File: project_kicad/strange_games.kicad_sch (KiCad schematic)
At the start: 156 parts, among them J1 Display, J2 Conn_02x02, J3 Conn_02x02, M1 Motor_DC, Q1 Q_Photo_NPN, Q2 Q_Photo_NPN, Q3 Si2302A, Q4 Si2302A, SW1 SW_Push, SW10 SW_Push, SW11 SW_Push, SW12 SW_Push, SW2 SW_Push, SW3 SW_Push, SW4 SW_Push, SW5 SW_Push, SW6 SW_Push, SW7 SW_Push, SW8 SW_Push, SW9 SW_Push, U1 STM32F446ZET6, U2 charge controller, U3 boost converter, U4 LDL1117S33R, U5 MQ-135 gas sensor, U6 ESP8266-01, U7 TMP112xxDRL, U8 LSM6DS3

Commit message: replaces stm32 with esp32
remade schematic, replacing stm32 with esp32, starting making pcb. Deleted projects for stm32 and esp8266
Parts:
- removed C10, C11, C12, C13, C14, C15, C16, C18, C19, C20, C42, C45, C6, C68, C7, C8: C_Generic, PCM_Capacitor_SMD_AKL:C_0402_1005Metric, symbol Library:C_Generic
- removed C17, C43, C66, C9: C_Generic, PCM_Capacitor_SMD_AKL:C_0805_2012Metric, symbol Library:C_Generic
- removed FB1: FerriteBead, Inductor_SMD:L_0805_2012Metric, symbol Library:FerriteBead
- removed J2, J3: Conn_02x02, Connector_PinHeader_2.54mm:PinHeader_2x02_P2.54mm_Vertical, symbol Library:Conn_02x03
- removed R1, R15, R19, R2, R22, R23, R24, R4, R5: 10k_0805, PCM_4ms_Resistor:R_0805_2012Metric, symbol Library:1.2k_0603
- removed U1: STM32F446ZET6, Package_QFP:LQFP-144_20x20mm_P0.5mm, symbol Library:STM32F446ZETx
- removed U6: ESP8266-01, SnapEDA Library:XCVR_ESP8266-01_ESP-01, symbol Library:ESP8266-01/ESP-01
- added C70, C71: C_Generic, PCM_Capacitor_SMD_AKL:C_0402_1005Metric, symbol Library:C_Generic
- added C72: C_Generic, PCM_Capacitor_SMD_AKL:C_0805_2012Metric, symbol Library:C_Generic
- added R43, R44, R45, R46, R47: 10k_0805, PCM_4ms_Resistor:R_0805_2012Metric, symbol Library:1.2k_0603
- added U10: vibrating_sensor, symbol Sensor:vibarting_sensor
- added U9: ESP32-DEVKIT-V1, SnapEDA Library:MODULE_ESP32_DEVKIT_V1, symbol ESP32-DEVKIT-V1:ESP32-DEVKIT-V1
- C1: footprint PCM_Capacitor_SMD_AKL:C_0402_1005Metric -> PCM_Capacitor_SMD_AKL:C_0805_2012Metric; Capacity 2.2uF -> 10uF; Display ?F -> (none)
- C3, C4: footprint PCM_Capacitor_SMD_AKL:C_0402_1005Metric -> PCM_Capacitor_SMD_AKL:C_0805_2012Metric; Capacity 0.1uF -> 10uF; Voltage 10V -> 6.3V
- Q1, Q2: value Q_Photo_NPN -> Q_Photo
- U5: footprint Library:MQ-135 gas sensor -> Connector_PinHeader_1.27mm:PinHeader_1x04_P1.27mm_Vertical
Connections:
- net +3.3VA is gone; now on net +3V3: C5.1
- net CS_lsm is gone; now on net +3V3: U8.12 (CS)
- net SCL_lsm is gone; now on net SCL: U8.13 (SCL)
- net SCL_tmp is gone; now on net SCL: U7.1 (SCL)
- net SDA_lsm is gone; now on net SDA: U8.14 (SDA)
- net +3V3: now also C1.2, C2.1, C4.2, U5.1 (VCC), C70.2, C71.1, C72.2, R43.2, R44.2, R45.2, R46.2, R47.2, U10.1 (VCC), U9.1 (3V3), U9.16 (EN); no longer C4.1, J1.3 (P/S), R13.2, U5.2 (VCC)
- net B1: now also U9.22 (D33)
- net B10: now also U9.12 (RX0)
- net B11: now also U9.18 (VN)
- net B12: now also U9.17 (VP)
- net B2: now also U9.21 (D32)
- net B3: now also U9.25 (D27)
- net B4: now also U9.24 (D26)
- net B5: now also U9.23 (D25)
- net B6: now also U9.15 (D23)
- net B7: now also U9.7 (TX2)
- net B8: now also U9.6 (RX2)
- net B9: now also U9.13 (TX0)
- net GND: now also C2.2, C4.1, J1.3 (P/S), R13.1, U5.2 (GND), C70.1, C71.2, C72.1, U10.2 (GND), U9.2 (GND), U9.29 (GND__1); no longer C2.1, C4.2, U5.1 (GND)
- net at D10.4 (DI): now also D9.1 (DO); no longer D7.1 (DO)
- net at D12.1 (DO): now also D9.4 (DI); no longer D7.4 (DI)
- net at D12.4 (DI): now also D7.1 (DO); no longer D9.1 (DO)
- net at D6.1 (DO): now also D7.4 (DI); no longer D9.4 (DI)
- net C15 renamed gas_signal
- net gas_signal: now also U9.26 (D14), U9.8 (D5)
- net C2 renamed open_box
- net open_box: now also U9.19 (D34)
- net D0 renamed A0_display
- net A0_display: now also R45.1, U9.3 (D15)
- net D1 renamed WR_display
- net WR_display: now also R46.1, U9.9 (D18)
- net D10 renamed SDA
- net SDA: now also U7.6 (SDA), R43.1, U9.11 (D21)
- net D2 renamed RD_display
- net RD_display: now also R47.1, U9.10 (D19)
- net D3: no longer names the net of J1.29 (D0)
- net D4: no longer names the net of J1.28 (D1)
- net D5: no longer names the net of J1.27 (D2)
- net D6: no longer names the net of J1.26 (D3)
- net D7: no longer names the net of J1.25 (D4)
- net D8: no longer names the net of J1.24 (D5)
- net D9 renamed SCL
- net SCL: now also R44.1, U9.14 (D22)
- removed net SDA_tmp: R13.1, U7.6 (SDA)
- net С0 renamed luminodiodes
- net luminodiodes: now also U9.4 (D2)
- net С1 renamed vibrating_motor
- net vibrating_motor: now also U9.20 (D35)
- net С3 renamed photo_1
- net photo_1: now also U9.28 (D13)
- net С4 renamed photo_2
- net photo_2: now also U9.27 (D12)
- new net vibrating_signal: R13.2, U10.3 (DO), U9.5 (D4)
- no-connect marks 7 -> 14
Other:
- note added: "ESP32 для управления всем кубиком и связи по wifi"
- note added: "датчики цифровые должны быть близко к ESP32 датчики света отдельно"
- note removed: "VBAT"
- note removed: "VDD"
- note removed: "VDDA"
- note removed: "esp8266 для бутлодера и общения по wi-fi"
- note removed: "stm32 для управления всей игрой"
- note removed: "датчики цифровые должны быть близко к stm32 датчики света отдельно"
- moved on the sheet: BT1, C21, C22, C23, C24, C25, C26, C27, C28, C29, C30, C31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

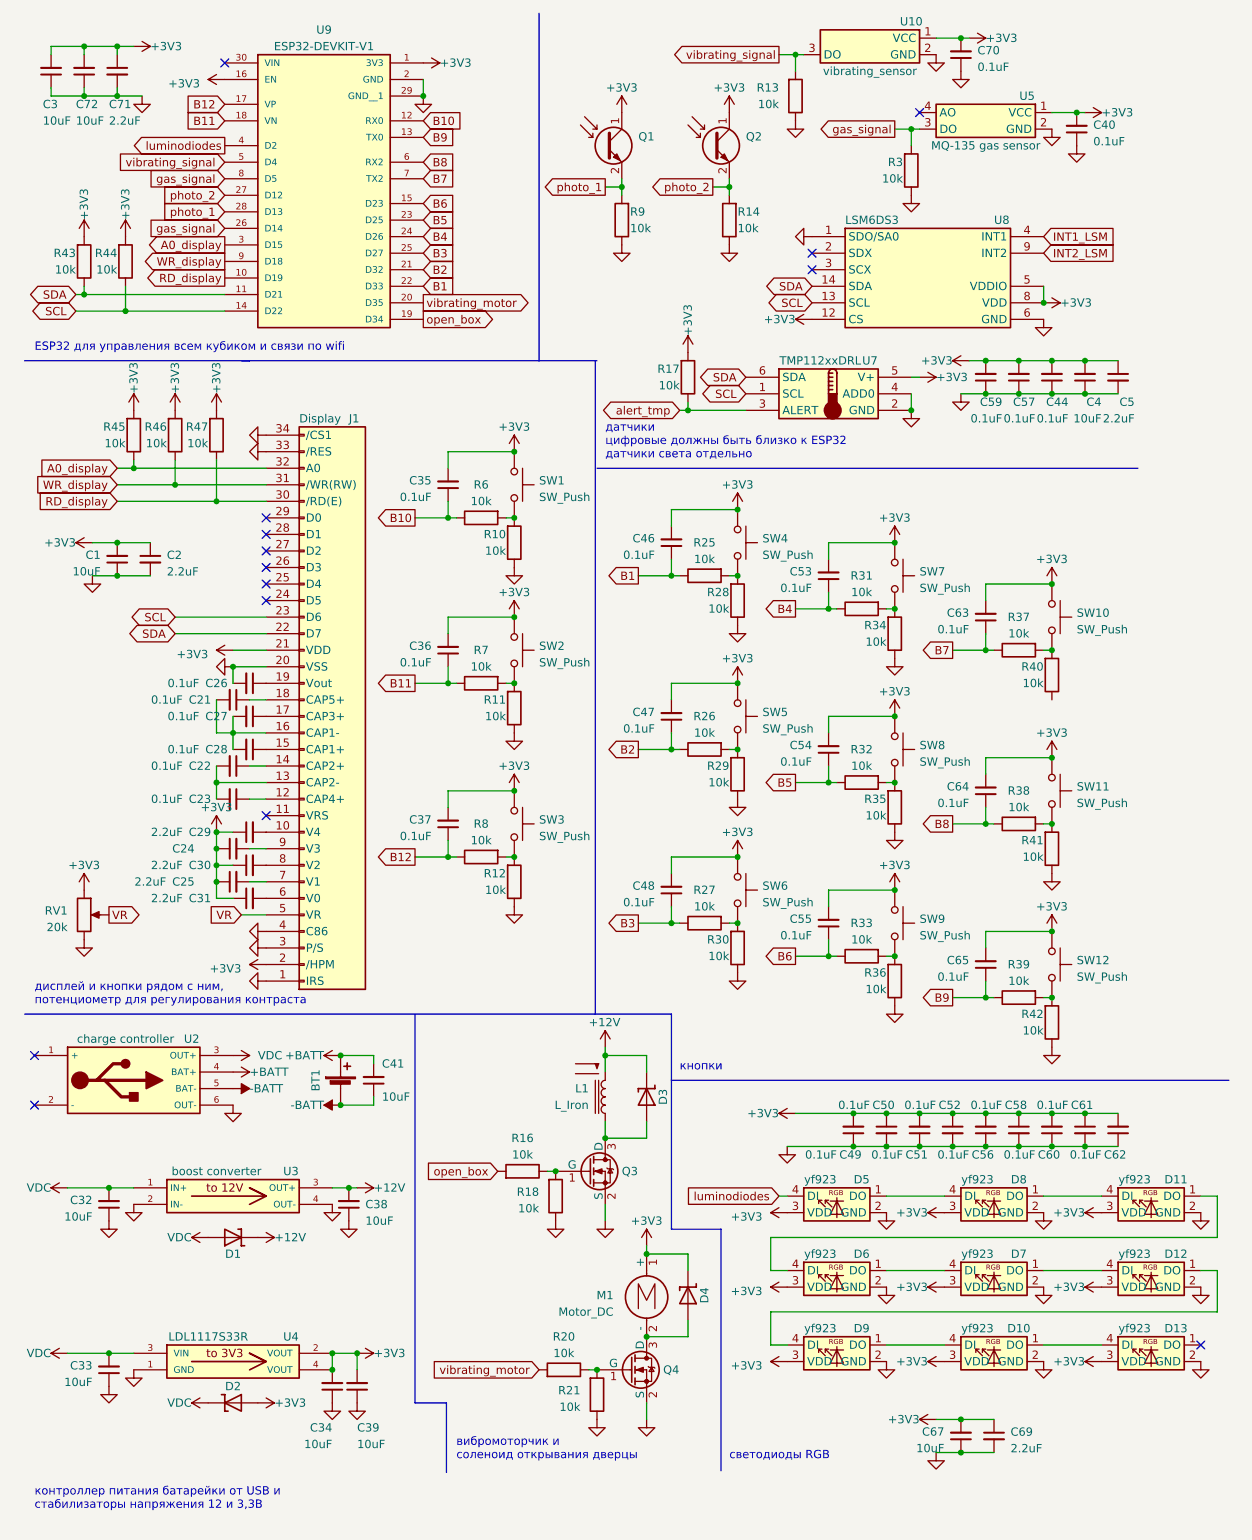
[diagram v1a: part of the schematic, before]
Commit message: updated components numbers
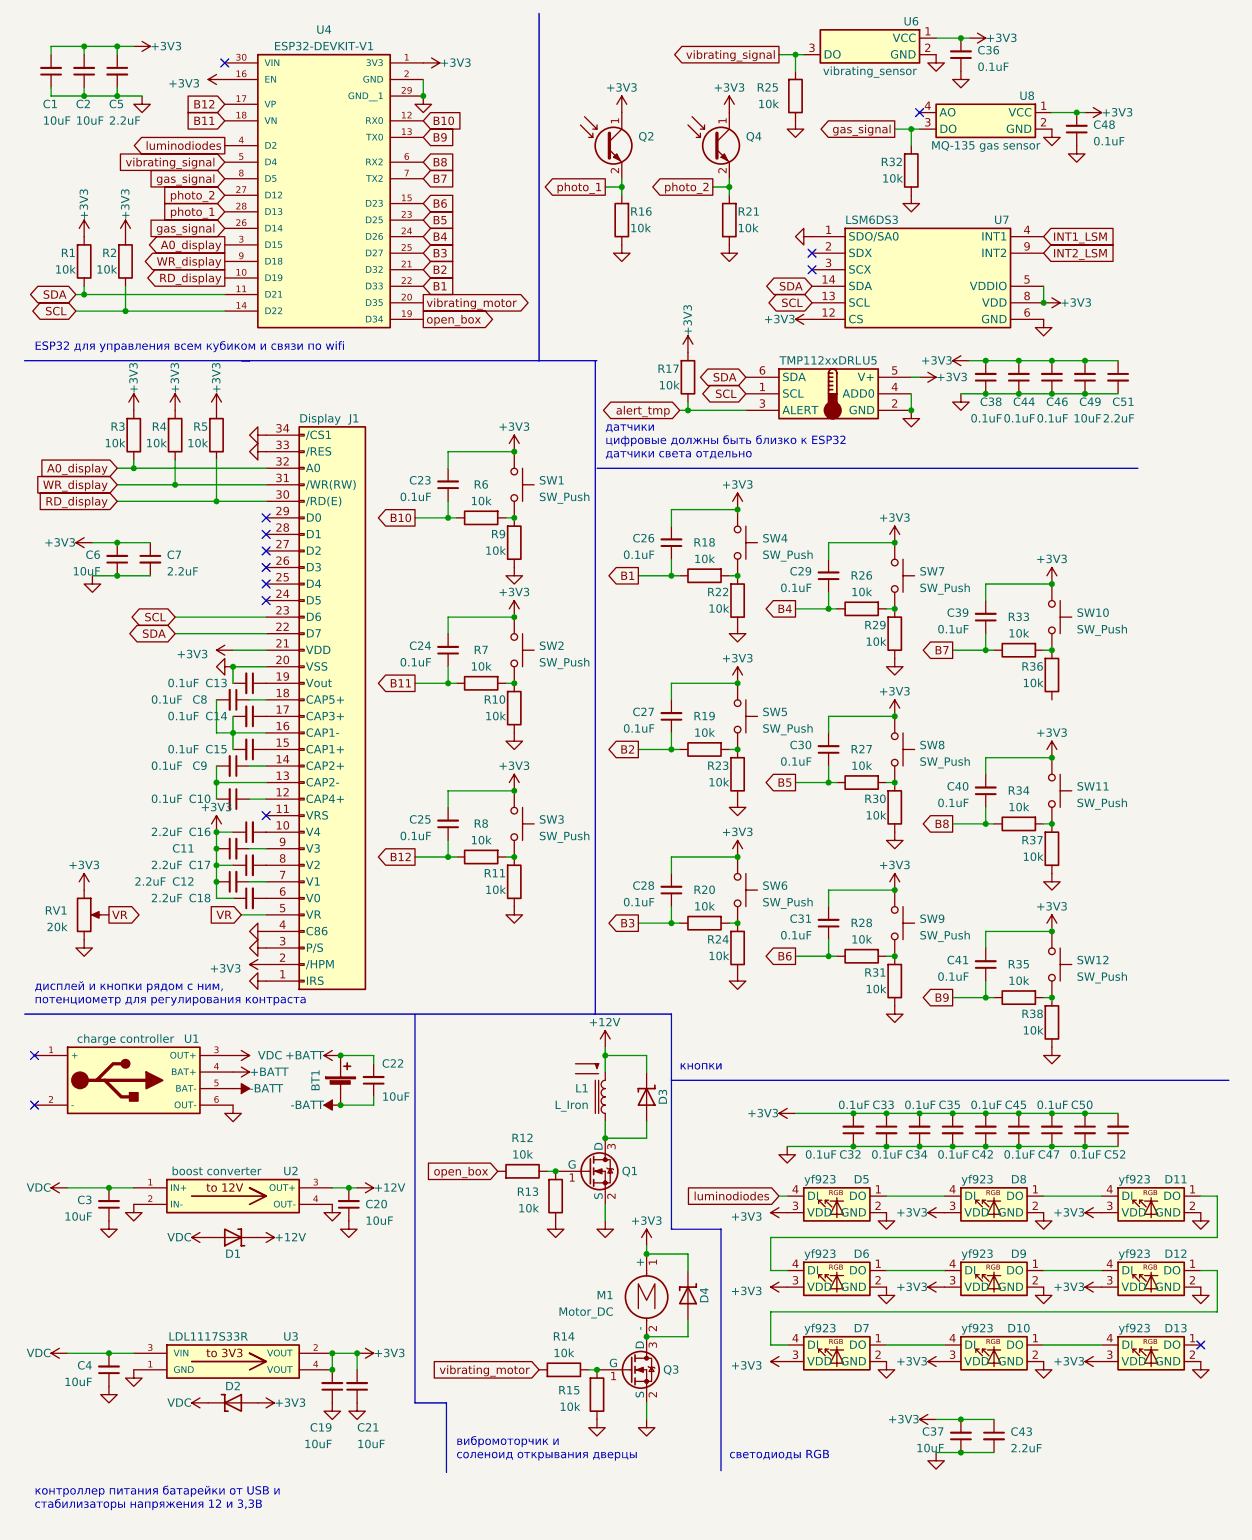
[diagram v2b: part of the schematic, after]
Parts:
- renumbered C3 to C1, C23 to C10, C24 to C11, C25 to C12, C26 to C13, C27 to C14, C28 to C15, C29 to C16, C30 to C17, C31 to C18, C34 to C19, C72 to C2, C38 to C20, C39 to C21, C41 to C22, C35 to C23, C36 to C24, C37 to C25, C46 to C26, C47 to C27, C48 to C28, C53 to C29, C32 to C3, C54 to C30, C55 to C31, C49 to C32, C50 to C33, C51 to C34, C52 to C35, C70 to C36, C67 to C37, C59 to C38, C63 to C39, C33 to C4, C64 to C40, C65 to C41, C56 to C42, C69 to C43, C57 to C44, C58 to C45, C44 to C46, C60 to C47, C40 to C48, C4 to C49, C71 to C5, C61 to C50, C5 to C51, C62 to C52, C1 to C6, C2 to C7, C21 to C8, C22 to C9, D9 to D7, D7 to D9, Q3 to Q1, Q1 to Q2, Q4 to Q3, Q2 to Q4, R43 to R1, R11 to R10, R12 to R11, R16 to R12, R18 to R13, R20 to R14, R21 to R15, R9 to R16, R25 to R18, R26 to R19, R44 to R2, R27 to R20, R14 to R21, R28 to R22, R29 to R23, R30 to R24, R13 to R25, R31 to R26, R32 to R27, R33 to R28, R34 to R29, R45 to R3, R35 to R30, R36 to R31, R3 to R32, R37 to R33, R38 to R34, R39 to R35, R40 to R36, R41 to R37, R42 to R38, R46 to R4, R47 to R5, R10 to R9, U2 to U1, U3 to U2, U4 to U3, U9 to U4, U7 to U5, U10 to U6, U8 to U7, U5 to U8

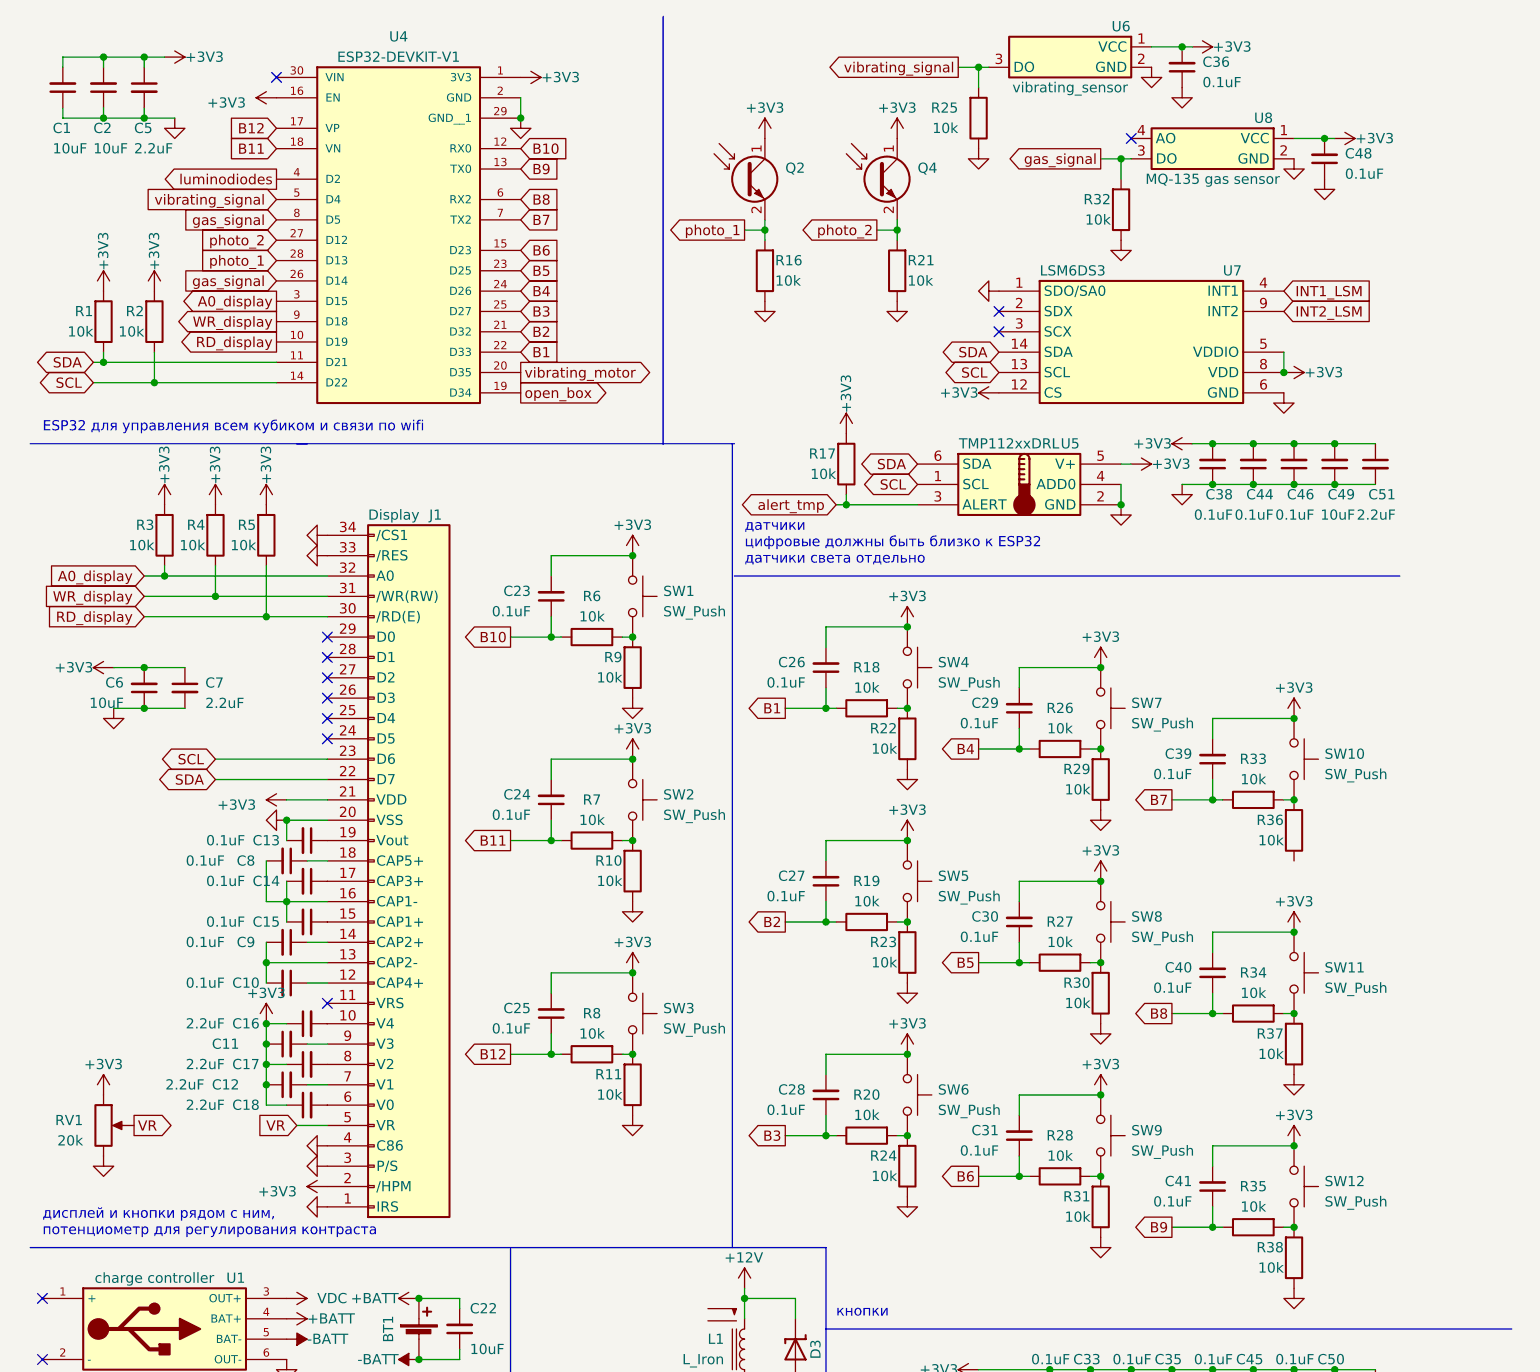
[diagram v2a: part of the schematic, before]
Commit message: deleted pins
deleted temperature alert pin and 2 buttons near the display because there are no enough pins in esp32
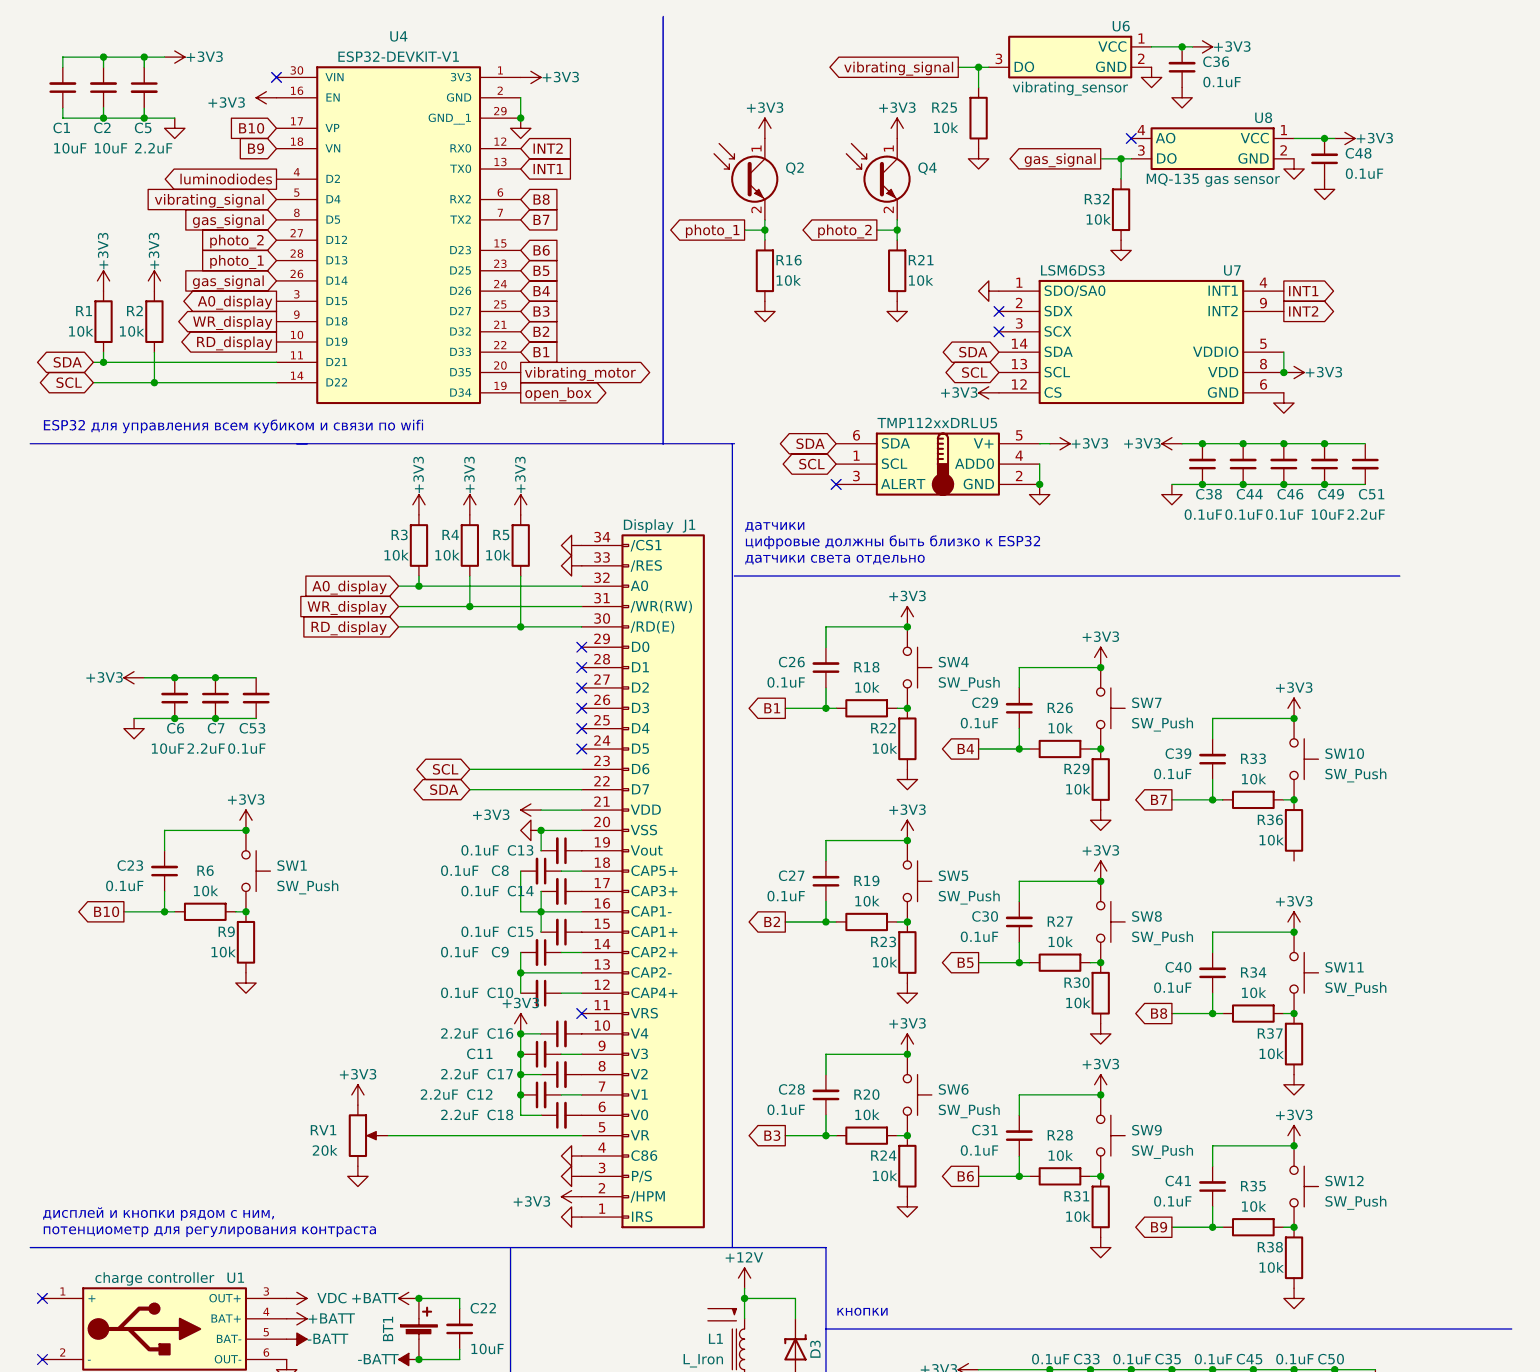
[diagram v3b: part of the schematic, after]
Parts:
- removed C24, C25: C_Generic, PCM_Capacitor_SMD_AKL:C_0402_1005Metric, symbol Library:C_Generic
- removed R10, R11, R17, R7, R8: 10k_0805, PCM_4ms_Resistor:R_0805_2012Metric, symbol Library:1.2k_0603
- removed SW2, SW3: SW_Push, Button_Switch_THT:SW_PUSH-12mm, symbol Switch:SW_Push
- added C53: C_Generic, PCM_Capacitor_SMD_AKL:C_0402_1005Metric, symbol Library:C_Generic
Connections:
- net B11 is gone; now on net B9: U4.18 (VN)
- net B12 is gone; now on net B10: U4.17 (VP)
- net +3V3: now also C53.2
- net B10: no longer U4.12 (RX0)
- net B9: no longer U4.13 (TX0)
- net GND: now also C53.1
- net INT1_LSM renamed INT1
- net INT1: now also U4.13 (TX0)
- net INT2_LSM renamed INT2
- net INT2: now also U4.12 (RX0)
- net VR: no longer names the net of J1.5 (VR), RV1.2
- net alert_tmp: no longer names the net of U5.3 (ALERT)
- no-connect marks 14 -> 15
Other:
- moved on the sheet: C10, C11, C12, C13, C14, C15, C16, C17, C18, C23, C38, C44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

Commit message: some more changes in sch
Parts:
- removed C22: C_Generic, PCM_Capacitor_SMD_AKL:C_0805_2012Metric, symbol Library:C_Generic
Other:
- note added: "к каждому входу питания"
- note added: "на всю группу"
- moved on the sheet: BT1, C19, C20, C21, C3, C37, C38, C4, C43, C44, C46, C49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
